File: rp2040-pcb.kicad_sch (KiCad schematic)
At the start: 43 parts, among them J1 Conn_01x20_Male, J2 Conn_01x20_Male, J3 USB_C_Receptacle, SW1 SW_Push, SW2 SW_Push, U1 TPS54202DDC, U2 W25Q128JVSIQ, U3 RP2040, Y1 12 MHz

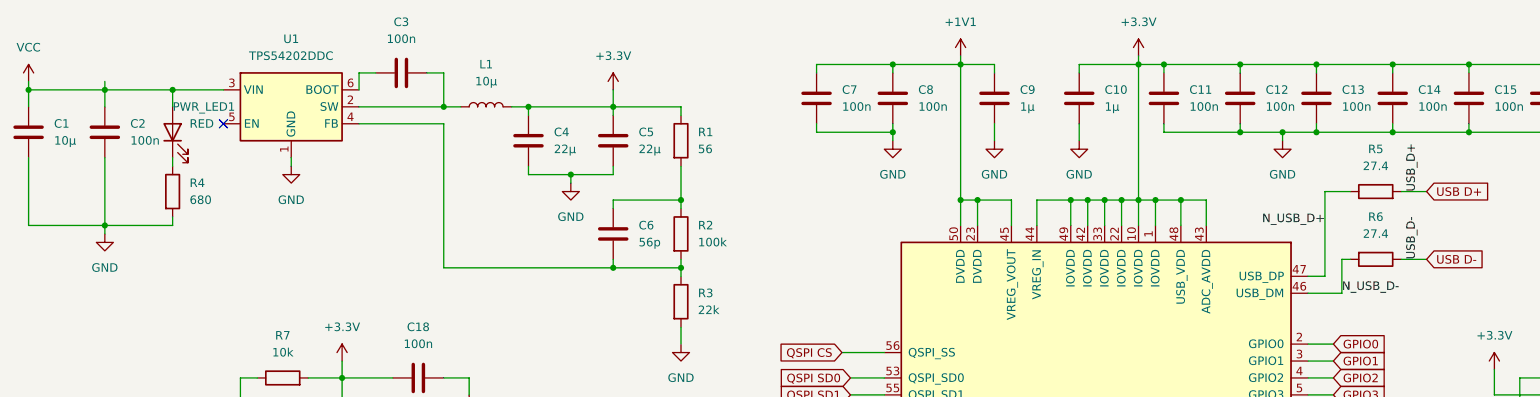
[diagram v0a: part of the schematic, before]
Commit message: Addressed electrical rules check-errors.
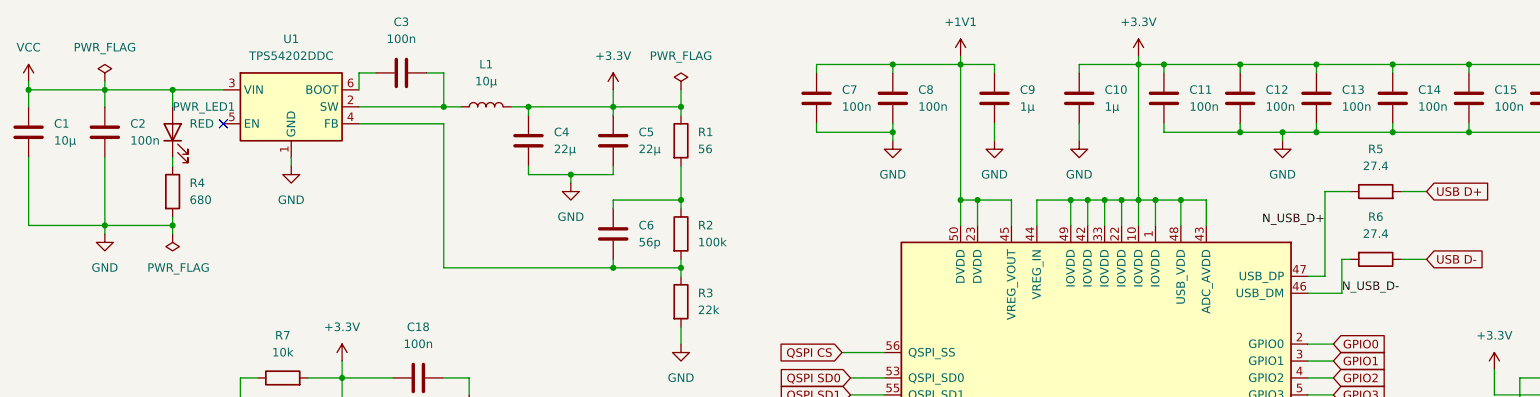
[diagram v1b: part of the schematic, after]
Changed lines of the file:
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@@
   (junction (at 80.01 170.18) (diameter 0) (color 0 0 0 0)
   )
+  (junction (at 114.3 33.02) (diameter 0) (color 0 0 0 0)
+  )
   (junction (at 91.44 33.02) (diameter 0) (color 0 0 0 0)
   )
@@
   )
   (junction (at 146.05 26.67) (diameter 0) (color 0 0 0 0)
+  )
+  (junction (at 38.1 50.8) (diameter 0) (color 0 0 0 0)
   )
   (junction (at 232.41 26.67) (diameter 0) (color 0 0 0 0)
@@
     (stroke (width 0) (type default) (color 0 0 0 0))
   )
+  (wire (pts (xy 38.1 50.8) (xy 38.1 52.07))
+    (stroke (width 0) (type default) (color 0 0 0 0))
+  )
   (wire (pts (xy 198.12 26.67) (xy 198.12 27.94))
     (stroke (width 0) (type default) (color 0 0 0 0))
@@
   )
   (wire (pts (xy 251.46 68.58) (xy 255.27 68.58))
+    (stroke (width 0) (type default) (color 0 0 0 0))
+  )
+  (wire (pts (xy 114.3 30.48) (xy 114.3 33.02))
     (stroke (width 0) (type default) (color 0 0 0 0))
   )
@@
     (effects (font (size 1.27 1.27)) (justify left bottom))
   )
-  (label "USB_D-" (at 224.79 55.88 90)
-    (effects (font (size 1.27 1.27)) (justify left bottom))
-  )
   (label "N_USB_D+" (at 210.82 50.8 180)
     (effects (font (size 1.27 1.27)) (justify right bottom))
-  )
-  (label "USB_D+" (at 224.79 45.72 90)
-    (effects (font (size 1.27 1.27)) (justify left bottom))
   )
   (global_label "GPIO16" (shape input) (at 251.46 106.68 180) (fields_autoplaced)
@@
     (pin "1")
   )
+  (symbol (lib_id "power:PWR_FLAG") (at 114.3 30.48 0) (unit 1)
+    (in_bom yes) (on_board yes) (fields_autoplaced)
+    (property "Reference" "#FLG02" (id 0) (at 114.3 28.575 0)
+      (effects (font (size 1.27 1.27)) hide)
+    )
+    (property "Value" "PWR_FLAG" (id 1) (at 114.3 25.4 0))
+    (property "Footprint" "" (id 2) (at 114.3 30.48 0)
+      (effects (font (size 1.27 1.27)) hide)
+    )
+    (property "Datasheet" "~" (id 3) (at 114.3 30.48 0)
+      (effects (font (size 1.27 1.27)) hide)
+    )
+    (pin "1")
+  )
   (symbol (lib_id "Memory_Flash:W25Q128JVS") (at 63.5 90.17 0) (unit 1)
     (in_bom yes) (on_board yes) (fields_autoplaced)
@@
     )
     (property "Datasheet" "" (id 3) (at 173.99 38.1 0)
+      (effects (font (size 1.27 1.27)) hide)
+    )
+    (pin "1")
+  )
+  (symbol (lib_id "power:PWR_FLAG") (at 38.1 52.07 180) (unit 1)
+    (in_bom yes) (on_board yes)
+    (property "Reference" "#FLG03" (id 0) (at 38.1 53.975 0)
+      (effects (font (size 1.27 1.27)) hide)
+    )
+    (property "Value" "PWR_FLAG" (id 1) (at 34.29 57.15 0)
+      (effects (font (size 1.27 1.27)) (justify right))
+    )
+    (property "Footprint" "" (id 2) (at 38.1 52.07 0)
+      (effects (font (size 1.27 1.27)) hide)
+    )
+    (property "Datasheet" "~" (id 3) (at 38.1 52.07 0)
       (effects (font (size 1.27 1.27)) hide)
     )
@@
     (pin "1")
     (pin "2")
+  )
+  (symbol (lib_id "power:PWR_FLAG") (at 27.94 29.21 0) (unit 1)
+    (in_bom yes) (on_board yes) (fields_autoplaced)
+    (property "Reference" "#FLG01" (id 0) (at 27.94 27.305 0)
+      (effects (font (size 1.27 1.27)) hide)
+    )
+    (property "Value" "PWR_FLAG" (id 1) (at 27.94 24.13 0))
+    (property "Footprint" "" (id 2) (at 27.94 29.21 0)
+      (effects (font (size 1.27 1.27)) hide)
+    )
+    (property "Datasheet" "~" (id 3) (at 27.94 29.21 0)
+      (effects (font (size 1.27 1.27)) hide)
+    )
+    (pin "1")
   )
   (symbol (lib_id "power:GND") (at 25.4 101.6 0) (unit 1)
@@
   )
   (symbol_instances
+    (path "/70545c5a-9a77-450f-b50a-82ea2fe4f006"
+      (reference "#FLG01") (unit 1) (value "PWR_FLAG") (footprint "")
+    )
+    (path "/3d37eced-ceb9-4eec-a597-c9aa7dc783bf"
+      (reference "#FLG02") (unit 1) (value "PWR_FLAG") (footprint "")
+    )
+    (path "/4967ff8f-d82d-4260-b6bc-147326dd1420"
+      (reference "#FLG03") (unit 1) (value "PWR_FLAG") (footprint "")
+    )
     (path "/24f86983-b1e1-4fd8-8935-6a20acfa9e5a"
       (reference "#PWR0101") (unit 1) (value "GND") (footprint "")

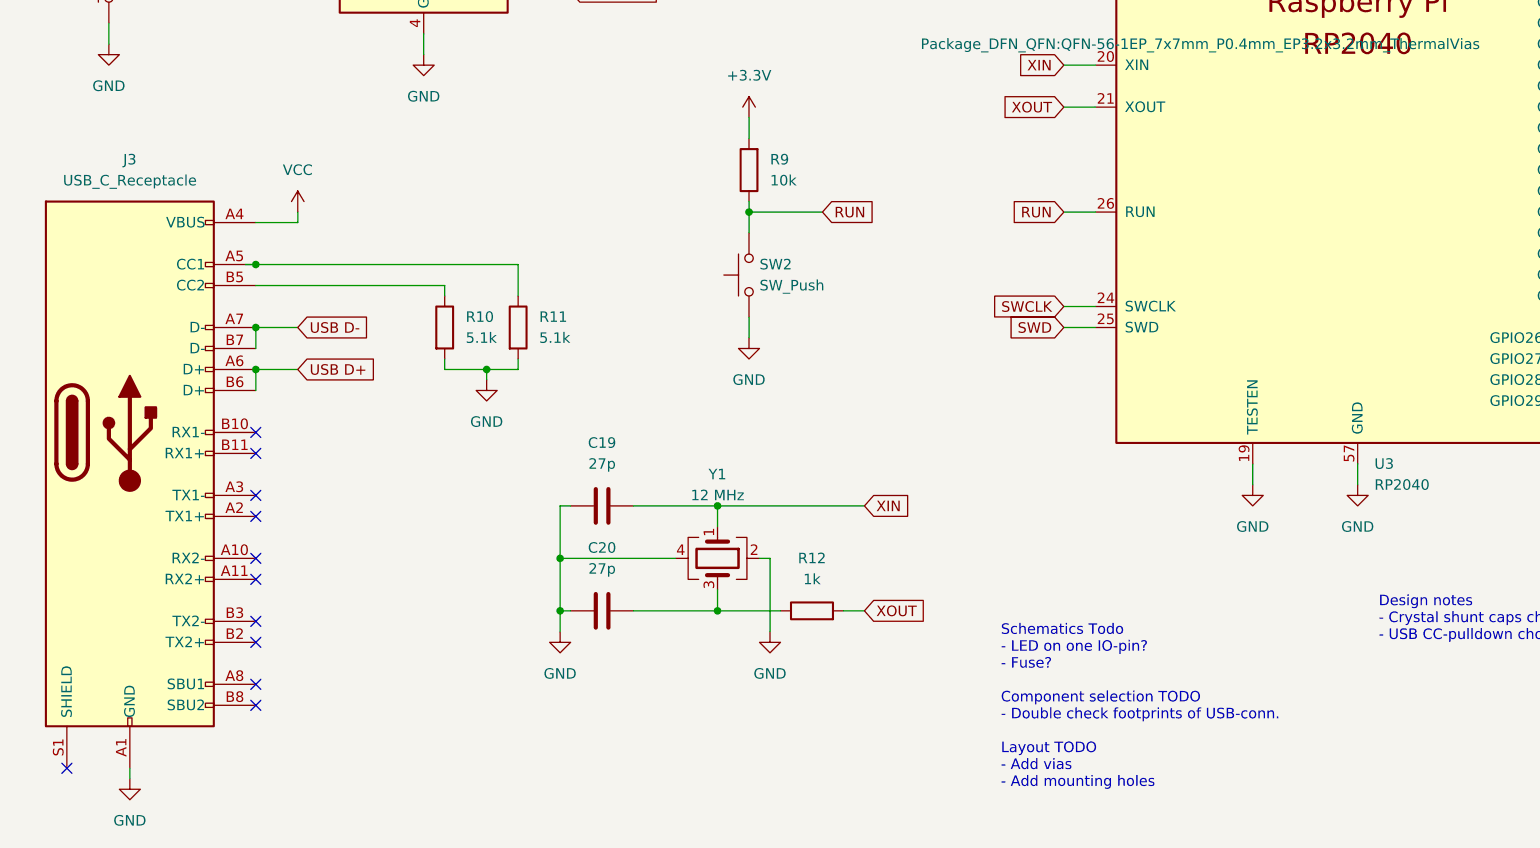
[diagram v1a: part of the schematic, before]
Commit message: Exchanged USB-receptacle. I could not find a footprint for the Chinese USB-receptacle I had chosen. Thus I selected one from Molex instead.
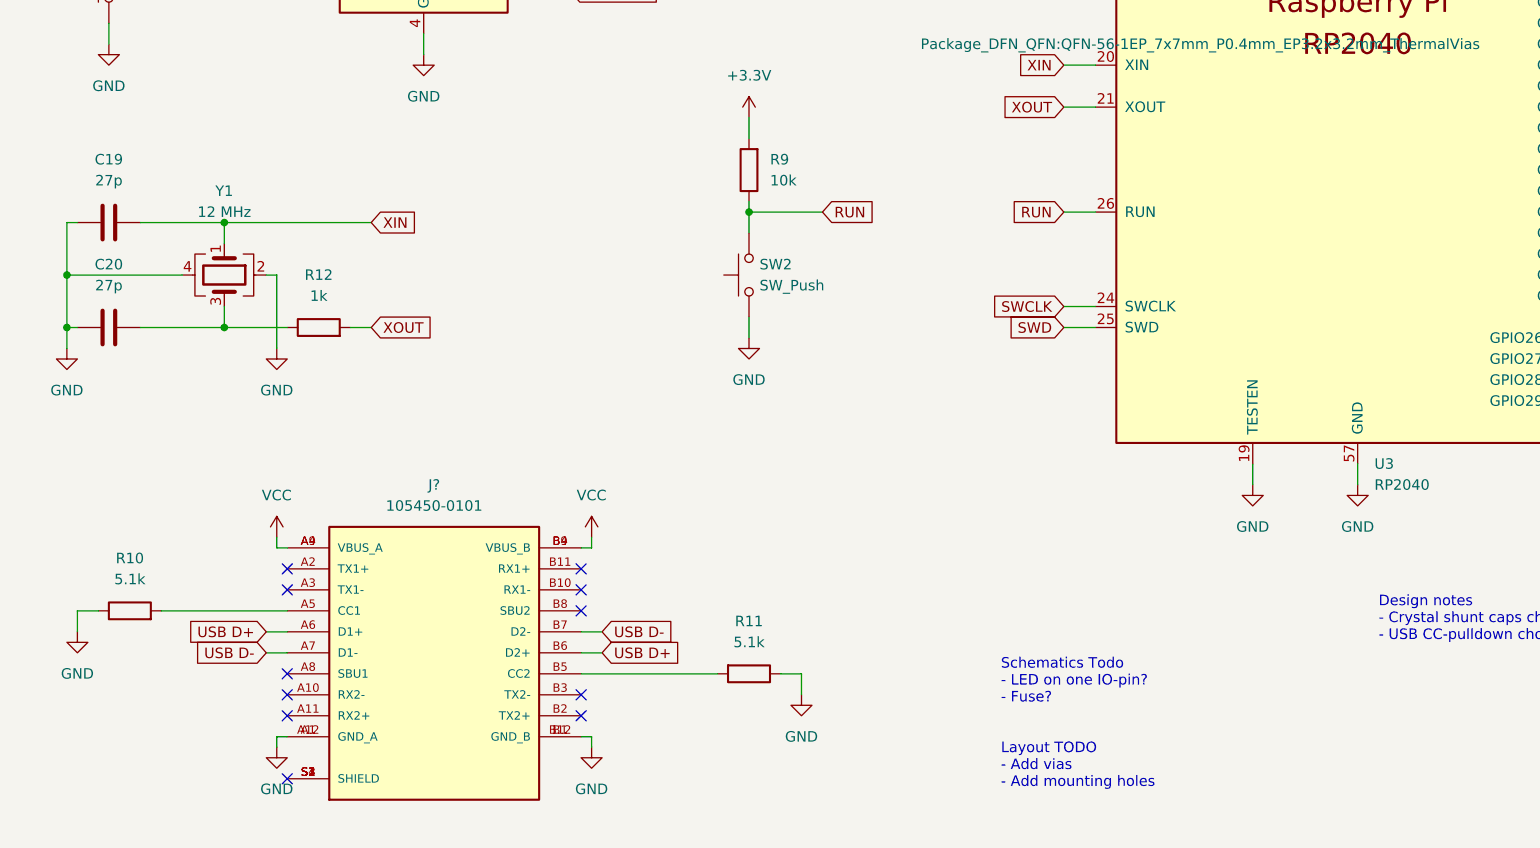
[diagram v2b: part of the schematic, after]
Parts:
- removed J3: USB_C_Receptacle, Connector_USB:USB_C_Receptacle_Palconn_UTC16-G, symbol Connector:USB_C_Receptacle
- added J?: 105450-0101, MOLEX_105450-0101, symbol 105450-0101:105450-0101
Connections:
- net GND: now also R10.1, R11.1, J?.A1 (GND_A), J?.A12 (GND_A), J?.B1 (GND_B), J?.B12 (GND_B); no longer R10.2, R11.2
- net USB D+: now also J?.A6 (D1+), J?.B6 (D2+)
- net USB D-: now also J?.A7 (D1-), J?.B7 (D2-)
- net VCC: now also J?.A4 (VBUS_A), J?.A9 (VBUS_A), J?.B4 (VBUS_B), J?.B9 (VBUS_B)
- new net: J?.A5 (CC1), R10.2
- new net: J?.B5 (CC2), R11.2
- new net: J?.S1 (SHIELD), J?.S2 (SHIELD), J?.S3 (SHIELD), J?.S4 (SHIELD)
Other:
- note added: "Schematics Todo - LED on one IO-pin? - Fuse? Layout TODO - Add vias - Add mounting holes"
- note removed: "Schematics Todo - LED on one IO-pin? - Fuse? Component selection TODO - Double check footprints of USB-conn. Layout TODO - Add vias - Add mounting holes"
- moved on the sheet: C19, C20, R10, R11, R12, Y1

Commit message: Generated net list
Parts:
- gave numbers to parts that had none: 1
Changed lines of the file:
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@@
   (symbol (lib_id "105450-0101:105450-0101") (at 64.77 175.26 0) (unit 1)
     (in_bom yes) (on_board yes) (fields_autoplaced)
-    (property "Reference" "J?" (id 0) (at 64.77 154.94 0))
+    (property "Reference" "J3" (id 0) (at 64.77 154.94 0))
     (property "Value" "105450-0101" (id 1) (at 64.77 157.48 0))
     (property "Footprint" "MOLEX_105450-0101" (id 2) (at 64.77 175.26 0)
@@
   (symbol (lib_id "power:GND") (at 45.72 186.69 0) (unit 1)
     (in_bom yes) (on_board yes) (fields_autoplaced)
-    (property "Reference" "#PWR?" (id 0) (at 45.72 193.04 0)
+    (property "Reference" "#PWR0135" (id 0) (at 45.72 193.04 0)
       (effects (font (size 1.27 1.27)) hide)
     )
@@
   (symbol (lib_id "power:GND") (at 21.59 172.72 0) (unit 1)
     (in_bom yes) (on_board yes) (fields_autoplaced)
-    (property "Reference" "#PWR?" (id 0) (at 21.59 179.07 0)
+    (property "Reference" "#PWR0108" (id 0) (at 21.59 179.07 0)
       (effects (font (size 1.27 1.27)) hide)
     )
@@
   (symbol (lib_id "power:VCC") (at 83.82 161.29 0) (unit 1)
     (in_bom yes) (on_board yes) (fields_autoplaced)
-    (property "Reference" "#PWR?" (id 0) (at 83.82 165.1 0)
+    (property "Reference" "#PWR0109" (id 0) (at 83.82 165.1 0)
       (effects (font (size 1.27 1.27)) hide)
     )
@@
   (symbol (lib_id "power:GND") (at 83.82 186.69 0) (unit 1)
     (in_bom yes) (on_board yes) (fields_autoplaced)
-    (property "Reference" "#PWR?" (id 0) (at 83.82 193.04 0)
+    (property "Reference" "#PWR0129" (id 0) (at 83.82 193.04 0)
       (effects (font (size 1.27 1.27)) hide)
     )
@@
   (symbol (lib_id "power:VCC") (at 45.72 161.29 0) (unit 1)
     (in_bom yes) (on_board yes) (fields_autoplaced)
-    (property "Reference" "#PWR?" (id 0) (at 45.72 165.1 0)
+    (property "Reference" "#PWR0134" (id 0) (at 45.72 165.1 0)
       (effects (font (size 1.27 1.27)) hide)
     )
@@
       (reference "#PWR0107") (unit 1) (value "GND") (footprint "")
     )
+    (path "/4d105bf4-e087-4582-a8fc-0bc73dc2df97"
+      (reference "#PWR0108") (unit 1) (value "GND") (footprint "")
+    )
+    (path "/84f07f6c-c66a-4813-92ee-2a95f5260d16"
+      (reference "#PWR0109") (unit 1) (value "VCC") (footprint "")
+    )
     (path "/907f772e-4afb-4233-98aa-60f2361366bc"
       (reference "#PWR0110") (unit 1) (value "GND") (footprint "")
@@
       (reference "#PWR0128") (unit 1) (value "+3.3V") (footprint "")
     )
+    (path "/e3a09f49-7b83-47b7-9cb1-3364c1815e55"
+      (reference "#PWR0129") (unit 1) (value "GND") (footprint "")
+    )
     (path "/c4b31e29-9e9b-4375-87ce-6e67b5ec718a"
       (reference "#PWR0130") (unit 1) (value "GND") (footprint "")
@@
       (reference "#PWR0133") (unit 1) (value "GND") (footprint "")
     )
+    (path "/edf5137e-8abc-462e-8a3b-7764e516cfe8"
+      (reference "#PWR0134") (unit 1) (value "VCC") (footprint "")
+    )
     (path "/14920ede-95b1-4085-8939-2faadab0dc6e"
-      (reference "#PWR?") (unit 1) (value "GND") (footprint "")
-    )
-    (path "/4d105bf4-e087-4582-a8fc-0bc73dc2df97"
-      (reference "#PWR?") (unit 1) (value "GND") (footprint "")
-    )
-    (path "/84f07f6c-c66a-4813-92ee-2a95f5260d16"
-      (reference "#PWR?") (unit 1) (value "VCC") (footprint "")
-    )
-    (path "/e3a09f49-7b83-47b7-9cb1-3364c1815e55"
-      (reference "#PWR?") (unit 1) (value "GND") (footprint "")
-    )
-    (path "/edf5137e-8abc-462e-8a3b-7764e516cfe8"
-      (reference "#PWR?") (unit 1) (value "VCC") (footprint "")
+      (reference "#PWR0135") (unit 1) (value "GND") (footprint "")
     )
     (path "/9c12fac9-f7f8-43f9-b443-23f3d244b6c0"
@@
     )
     (path "/02cde107-2275-4138-965a-0f862abdc842"
-      (reference "J?") (unit 1) (value "105450-0101") (footprint "MOLEX_105450-0101")
+      (reference "J3") (unit 1) (value "105450-0101") (footprint "MOLEX_105450-0101")
     )
     (path "/5d1ad0d0-d77a-4a68-aca6-47a066747d53"

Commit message: Started routing.
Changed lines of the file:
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@@
   (symbol (lib_id "105450-0101:105450-0101") (at 64.77 175.26 0) (unit 1)
     (in_bom yes) (on_board yes) (fields_autoplaced)
-    (property "Reference" "J3" (id 0) (at 64.77 154.94 0))
-    (property "Value" "105450-0101" (id 1) (at 64.77 157.48 0))
-    (property "Footprint" "MOLEX_105450-0101" (id 2) (at 64.77 175.26 0)
+    (property "Reference" "J3" (id 0) (at 64.77 157.48 0))
+    (property "Value" "105450-0101" (id 1) (at 64.77 160.02 0))
+    (property "Footprint" "MOLEX_105450-0101" (id 2) (at 88.9 179.07 0)
       (effects (font (size 1.27 1.27)) (justify bottom) hide)
     )
-    (property "Datasheet" "" (id 3) (at 64.77 175.26 0)
+    (property "Datasheet" "" (id 3) (at 64.77 153.67 0)
       (effects (font (size 1.27 1.27)) hide)
     )
-    (property "PARTREV" "A7" (id 4) (at 64.77 175.26 0)
+    (property "PARTREV" "A7" (id 4) (at 80.01 184.15 0)
       (effects (font (size 1.27 1.27)) (justify bottom) hide)
     )
-    (property "STANDARD" "Manufacturer Recommendations" (id 5) (at 64.77 175.26 0)
+    (property "STANDARD" "Manufacturer Recommendations" (id 5) (at 93.98 181.61 0)
       (effects (font (size 1.27 1.27)) (justify bottom) hide)
     )
-    (property "MAXIMUM_PACKAGE_HEIGHT" "3.24mm" (id 6) (at 64.77 175.26 0)
+    (property "MAXIMUM_PACKAGE_HEIGHT" "3.24mm" (id 6) (at 92.71 184.15 0)
       (effects (font (size 1.27 1.27)) (justify bottom) hide)
     )
-    (property "MANUFACTURER" "Molex" (id 7) (at 64.77 175.26 0)
+    (property "MANUFACTURER" "Molex" (id 7) (at 85.09 184.15 0)
       (effects (font (size 1.27 1.27)) (justify bottom) hide)
     )
